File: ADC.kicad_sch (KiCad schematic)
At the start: 23 parts, among them IC301 TLA2518IRTER, K301 FTR-B3GA4.5Z-B10, K302 FTR-B3GA4.5Z-B10, Q301 BC817

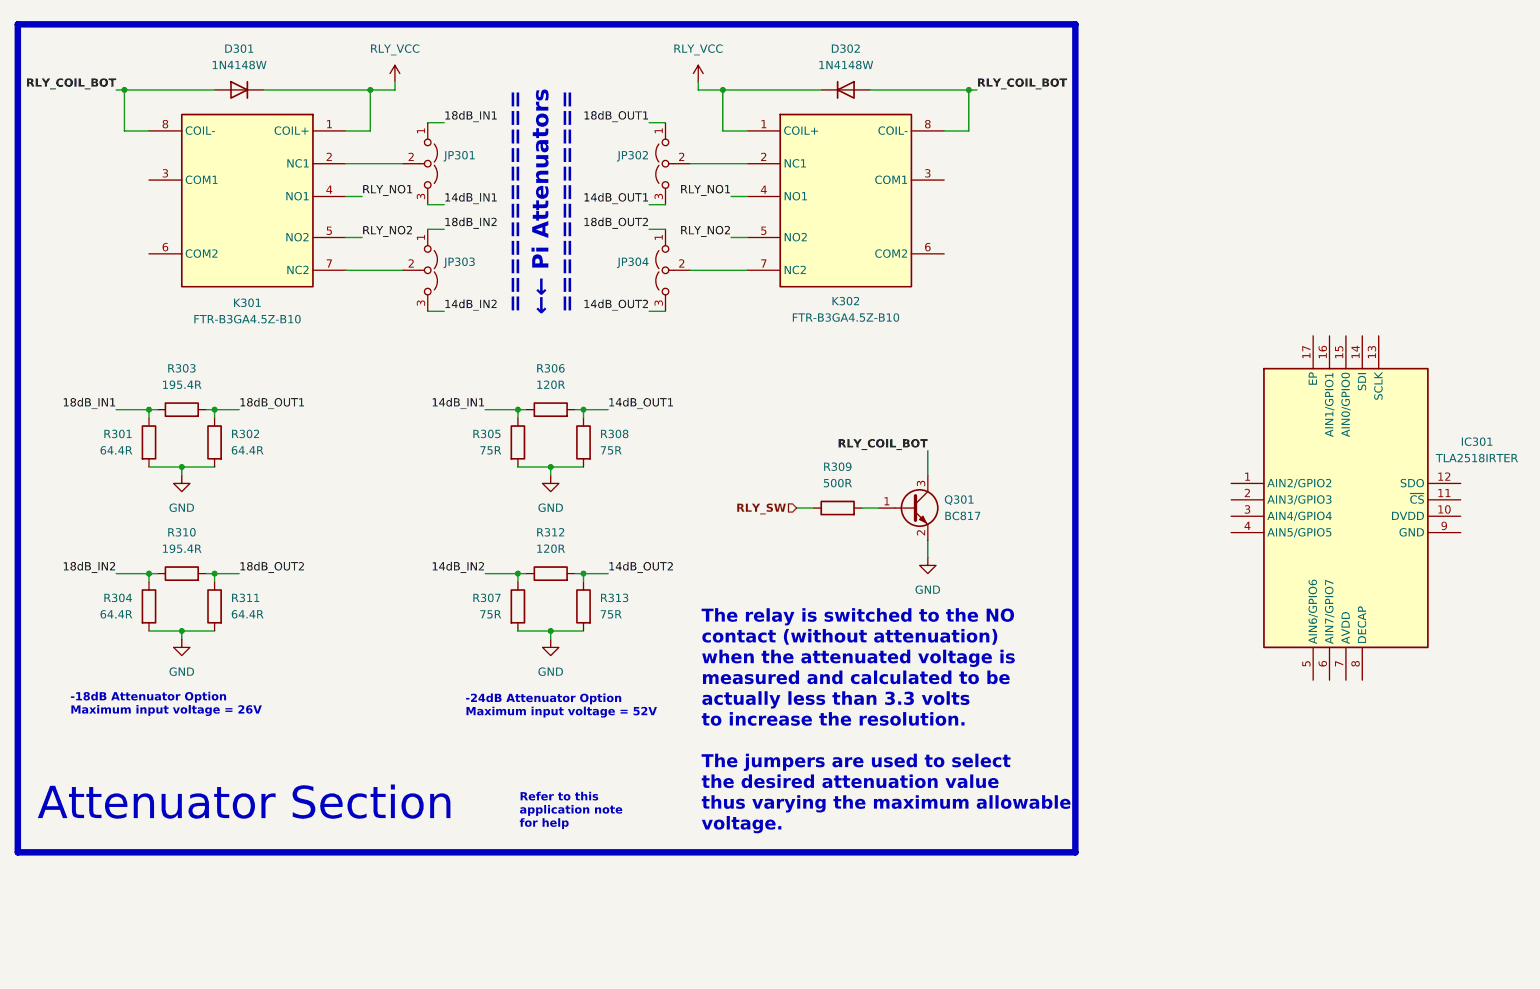
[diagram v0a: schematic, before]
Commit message: increased attenuation settings to 4 but decreased channels to 1
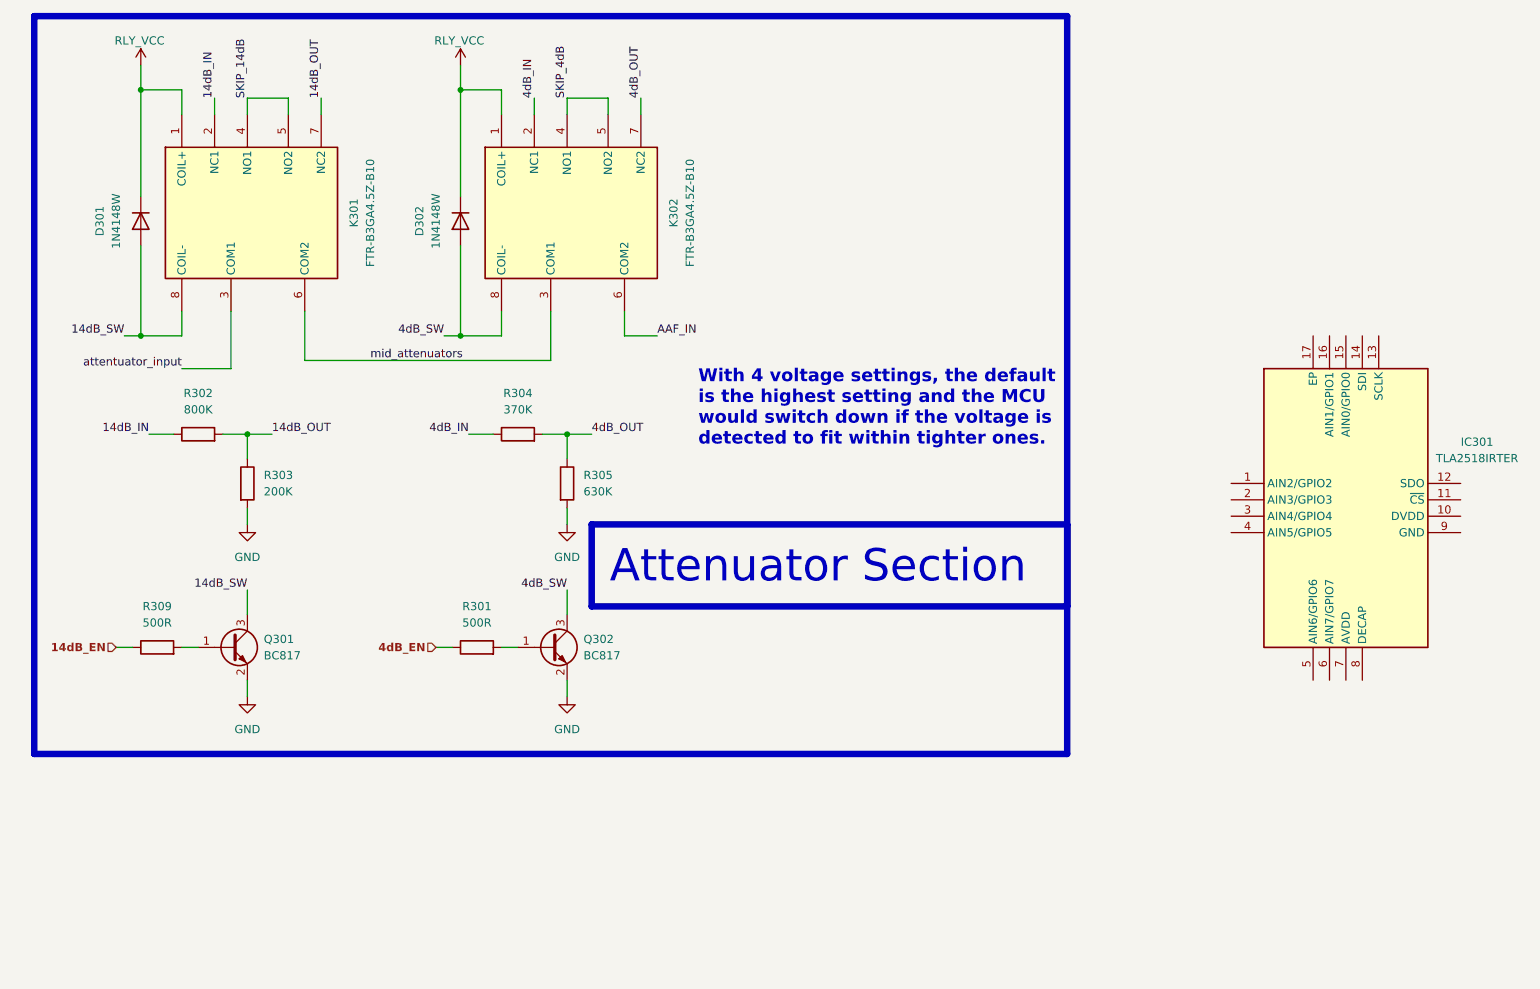
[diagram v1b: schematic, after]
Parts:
- removed JP301, JP302, JP303, JP304: Jumper_3_Open, symbol Jumper:Jumper_3_Open
- removed R306, R312: 120R, symbol Device:R
- removed R307, R308, R313: 75R, symbol Device:R
- removed R310: 195.4R, symbol Device:R
- removed R311: 64.4R, symbol Device:R
- added Q302: BC817, Package_TO_SOT_SMD:SOT-23, symbol Transistor_BJT:BC817
- R301: value 64.4R -> 500R
- R302: value 64.4R -> 800K
- R303: value 195.4R -> 200K
- R304: value 64.4R -> 370K
- R305: value 75R -> 630K
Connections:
- net 14dB_IN1 is gone; now on net 4dB_OUT: R305.1
- net 18dB_IN2 is gone; now on net 4dB_IN: R304.1
- net GND: now also R303.2, Q302.2 (E); no longer R301.2, R302.2, R304.2
- net 14dB_IN: now reaches K301.2 (NC1)
- net 14dB_IN: now also R302.1
- net 4dB_OUT: now reaches K302.7 (NC2)
- net 4dB_OUT: now also R304.2
- net 4dB_IN: now reaches K302.2 (NC1)
- net mid_attenuators: now reaches K302.3 (COM1)
- net mid_attenuators: now also K301.6 (COM2)
- net AAF_IN: now reaches K302.6 (COM2)
- net attentuator_input: now reaches K301.3 (COM1)
- net 14dB_OUT: now reaches K301.7 (NC2)
- net 14dB_OUT: now also R302.2, R303.1
- net 18dB_IN1 renamed 4dB_EN
- net 4dB_EN: no longer R303.1
- removed net 18dB_OUT1: R302.1, R303.2
- net RLY_COIL_BOT renamed 14dB_SW
- net 14dB_SW: no longer D302.2 (A), K302.8 (COIL-)
- net RLY_NO1 renamed SKIP_14dB
- net SKIP_14dB: now also K301.5 (NO2); no longer K302.4 (NO1)
- net RLY_NO2 renamed SKIP_4dB
- net SKIP_4dB: now also K302.4 (NO1); no longer K301.5 (NO2)
- net RLY_SW renamed 14dB_EN
- new net: Q302.1 (B), R301.2
- new net 4dB_SW: D302.2 (A), K302.8 (COIL-), Q302.3 (C)
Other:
- note added: "With 4 voltage settings, the default is the highest setting and the MCU would switch down if the voltage is detected to fit within tighter ones."
- note removed: "-18dB Attenuator Option Maximum input voltage = 26V"
- note removed: "-24dB Attenuator Option Maximum input voltage = 52V"
- note removed: "============ ←← Pi Attenuators ============"
- note removed: "Refer to this application note for help"
- note removed: "The relay is switched to the NO contact (without attenuation) when the attenuated voltage is measured and calculated to be actually less than 3.3 volts to increase the resolution. The jumpers are used to select the desired attenuation value thus varying the maximum allowable voltage."
- moved on the sheet: D301, K301, Q301, R309

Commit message: finished ADC side, may add some additional bare channels, started DAC part and need to add the tca0372 amplifier or think about it
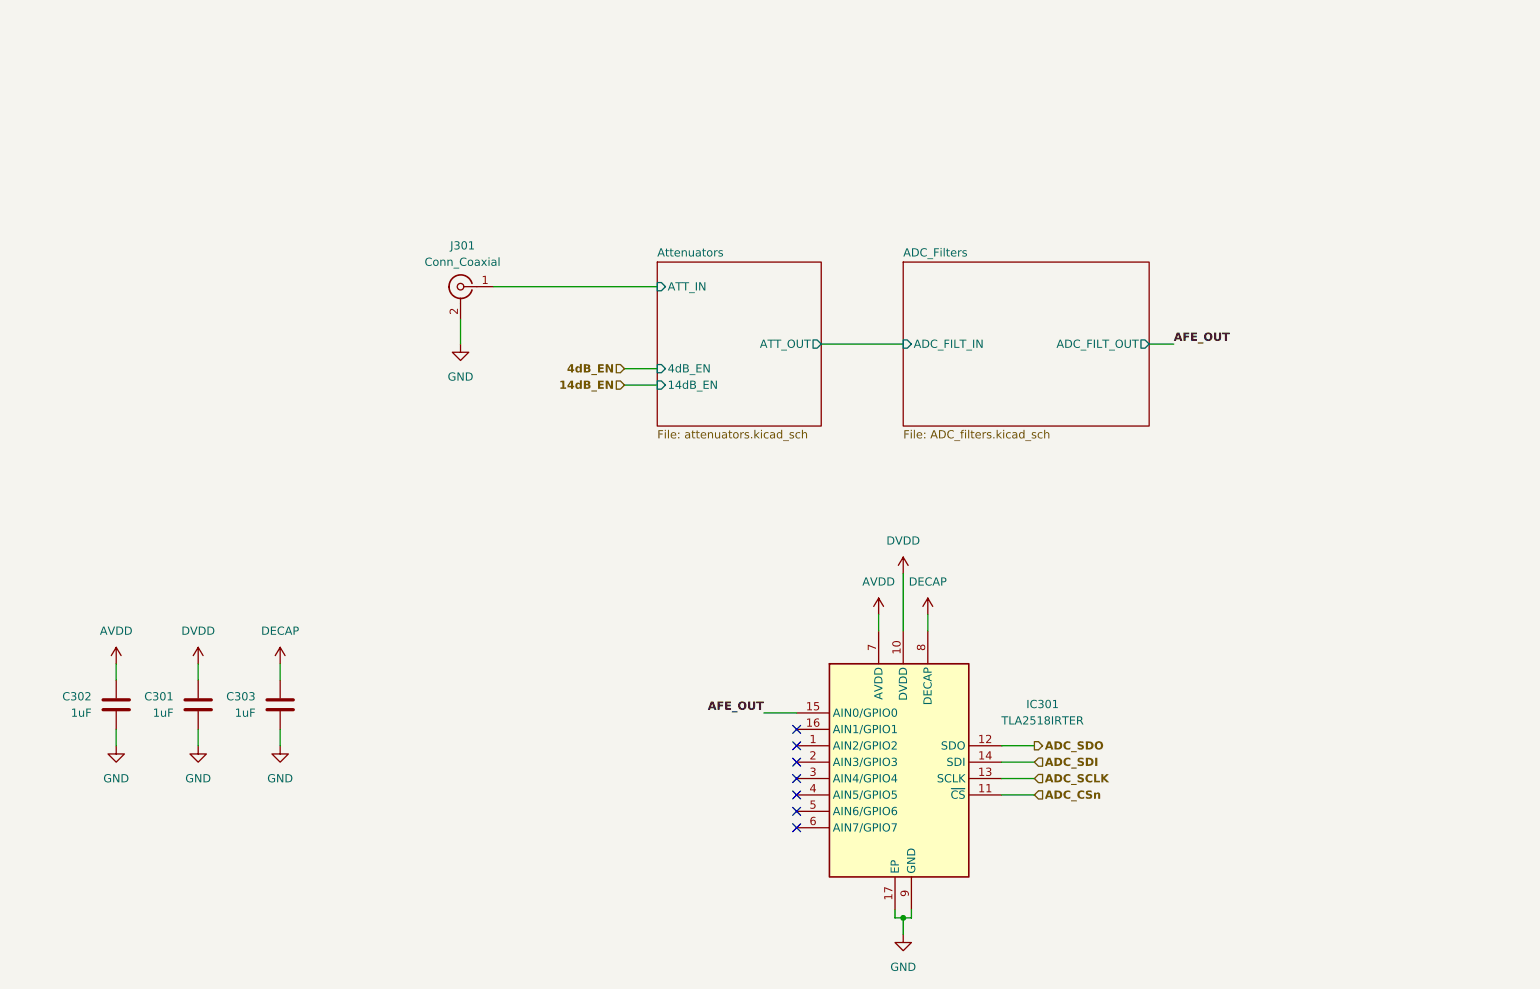
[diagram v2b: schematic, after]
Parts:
- removed D301, D302: 1N4148W, Diode_SMD:D_SOD-123, symbol Diode:1N4148W
- removed K301, K302: FTR-B3GA4.5Z-B10, FTRB3GA45ZB10, symbol FTR-B3GA4_5Z-B10:FTR-B3GA4.5Z-B10
- removed Q301, Q302: BC817, Package_TO_SOT_SMD:SOT-23, symbol Transistor_BJT:BC817
- removed R301, R309: 500R, symbol Device:R
- removed R302: 800K, symbol Device:R
- removed R303: 200K, symbol Device:R
- removed R304: 370K, symbol Device:R
- removed R305: 630K, symbol Device:R
- added C301, C302, C303: 1uF, symbol Device:C
- added J301: Conn_Coaxial, symbol Connector:Conn_Coaxial
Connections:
- net GND: now also IC301.17 (EP), IC301.9 (GND), C301.2, C302.2, C303.2, J301.2 (Ext)
- net DVDD: now reaches IC301.10 (DVDD)
- net DVDD: now also C301.1
- net ADC_CSn: now reaches IC301.11 (~{CS})
- net ADC_SDO: now reaches IC301.12 (SDO)
- net ADC_SCLK: now reaches IC301.13 (SCLK)
- net ADC_SDI: now reaches IC301.14 (SDI)
- net AFE_OUT: now reaches IC301.15 (AIN0/GPIO0)
- net AVDD: now reaches IC301.7 (AVDD)
- net AVDD: now also C302.1
- net DECAP: now reaches IC301.8 (DECAP)
- net DECAP: now also C303.1
- new net Attenuators/ATT_IN: J301.1 (In)
- no-connect marks 0 -> 7
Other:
- added sheet ADC_Filters (ADC_filters.kicad_sch)
- added sheet Attenuators (attenuators.kicad_sch)
- note removed: "Attenuator Section"
- note removed: "With 4 voltage settings, the default is the highest setting and the MCU would switch down if the voltage is detected to fit within tighter ones."
- moved on the sheet: IC301

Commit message: 80% done, maybe add more AINs, finish the power circuit and add system & block diagrams
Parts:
- added JP301: AIN Selector, symbol Jumper:Jumper_3_Open
- J301: value Conn_Coaxial -> ADC AFE IN
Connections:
- net AFE_OUT: now also JP301.3 (B)
- new net ADC_Filters/ADC_FILT_OUT: JP301.2 (C)
- new net MCU_ADC: JP301.1 (A)
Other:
- note added: "ADC Section"
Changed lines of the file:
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@@
 		(comment 2 "This sheet contains the input analog section for the NadyScope, including the attenuators,")
+	)
+	(text "ADC Section"
+		(exclude_from_sim no)
+		(at 52.324 22.606 0)
+		(effects
+			(font
+				(size 6 6)
+				(thickness 1.2)
+				(bold yes)
+			)
+		)
 	)
 	(junction
@@
 	(wire
 		(pts
+			(xy 198.12 57.15) (xy 198.12 54.61)
+		)
+		(stroke
+			(width 0)
+			(type default)
+		)
+	)
+	(wire
+		(pts
+			(xy 55.88 113.03) (xy 55.88 115.57)
+		)
+		(stroke
+			(width 0)
+			(type default)
+		)
+	)
+	(wire
+		(pts
+			(xy 148.59 105.41) (xy 148.59 107.95)
+		)
+		(stroke
+			(width 0)
+			(type default)
+		)
+	)
+	(wire
+		(pts
+			(xy 167.64 128.27) (xy 172.72 128.27)
+		)
+		(stroke
+			(width 0)
+			(type default)
+		)
+	)
+	(wire
+		(pts
 			(xy 190.5 63.5) (xy 194.31 63.5)
 		)
@@
 	(wire
 		(pts
-			(xy 55.88 113.03) (xy 55.88 115.57)
-		)
-		(stroke
-			(width 0)
-			(type default)
-		)
-	)
-	(wire
-		(pts
-			(xy 148.59 105.41) (xy 148.59 107.95)
-		)
-		(stroke
-			(width 0)
-			(type default)
-		)
-	)
-	(wire
-		(pts
-			(xy 167.64 128.27) (xy 172.72 128.27)
-		)
-		(stroke
-			(width 0)
-			(type default)
-		)
-	)
-	(wire
-		(pts
 			(xy 43.18 123.19) (xy 43.18 125.73)
 		)
@@
 	(wire
 		(pts
+			(xy 198.12 54.61) (xy 201.93 54.61)
+		)
+		(stroke
+			(width 0)
+			(type default)
+		)
+	)
+	(wire
+		(pts
 			(xy 151.13 151.13) (xy 151.13 152.4)
 		)
@@
 	(wire
 		(pts
+			(xy 198.12 72.39) (xy 198.12 69.85)
+		)
+		(stroke
+			(width 0)
+			(type default)
+		)
+	)
+	(wire
+		(pts
 			(xy 156.21 105.41) (xy 156.21 107.95)
+		)
+		(stroke
+			(width 0)
+			(type default)
+		)
+	)
+	(wire
+		(pts
+			(xy 201.93 72.39) (xy 198.12 72.39)
 		)
 		(stroke
@@
 	)
 	(label "AFE_OUT"
-		(at 194.31 63.5 0)
+		(at 201.93 72.39 0)
 		(effects
 			(font
@@
 				(thickness 0.254)
 				(bold yes)
+			)
+			(justify left)
+		)
+	)
+	(hierarchical_label "MCU_ADC"
+		(shape output)
+		(at 201.93 54.61 0)
+		(effects
+			(font
+				(size 1.27 1.27)
 			)
 			(justify left)
@@
 			)
 		)
-		(property "Value" "Conn_Coaxial"
+		(property "Value" "ADC AFE IN"
 			(at 84.1374 50.8 0)
 			(effects
@@
 					(unit 1)
 				)
+			)
+		)
+	)
+	(symbol
+		(lib_id "Jumper:Jumper_3_Open")
+		(at 198.12 63.5 270)
+		(unit 1)
+		(exclude_from_sim no)
+		(in_bom no)
+		(on_board yes)
+		(dnp no)
+		(fields_autoplaced yes)
+		(property "Reference" "JP301"
+			(at 200.66 62.2299 90)
+			(effects
+				(font
+					(size 1.27 1.27)
+				)
+				(justify left)
+			)
+		)
+		(property "Value" "AIN Selector"
+			(at 200.66 64.7699 90)
+			(effects
+				(font
+					(size 1.27 1.27)
+				)
+				(justify left)
+			)
+		)
+		(property "Footprint" ""
+			(at 198.12 63.5 0)
+			(effects
+				(font
+					(size 1.27 1.27)
+				)
+				(hide yes)
+			)
+		)
+		(property "Datasheet" "~"
+			(at 198.12 63.5 0)
+			(effects
+				(font
+					(size 1.27 1.27)
+				)
+				(hide yes)
+			)
+		)
+		(property "Description" "Jumper, 3-pole, both open"
+			(at 198.12 63.5 0)
+			(effects
+				(font
+					(size 1.27 1.27)
+				)
+				(hide yes)
+			)
+		)
+		(pin "1"
+		)
+		(pin "3"
+		)
+		(pin "2"
+		)
+		(instances
+			(project "NadyScope"
+				(path "/eb93e2be-0074-48a1-b88c-5129bddcbd28/34aa89fc-41cb-4285-a98d-3f26cd383eea"
+					(reference "JP301")
+					(unit 1)
+				)
